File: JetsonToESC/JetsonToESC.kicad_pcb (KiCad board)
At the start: 2 copper layers, 70 x 50 mm, 37 parts, among them J1 Conn_01x12, J2 Conn_01x03, J3 Conn_01x02, J4 Screw_Terminal_01x01, J5 Screw_Terminal_01x01, U1 ESP32-C3_SUPERMINI_TH, U2 DS18B20, U3 LMR51420XDDCR, U4 MCP23018x-x-SS, U5 ACS759xCB-100B-PFF

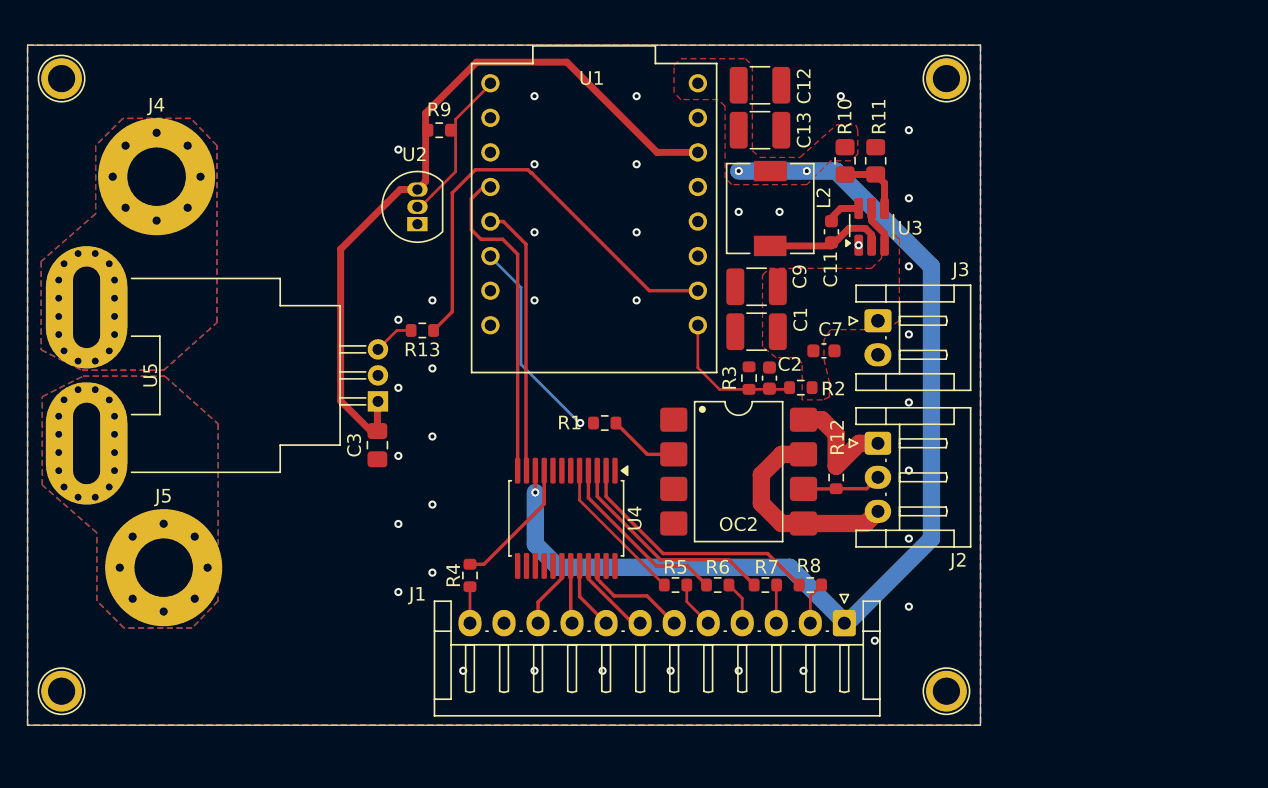
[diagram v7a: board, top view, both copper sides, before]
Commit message: Edit around current sensor
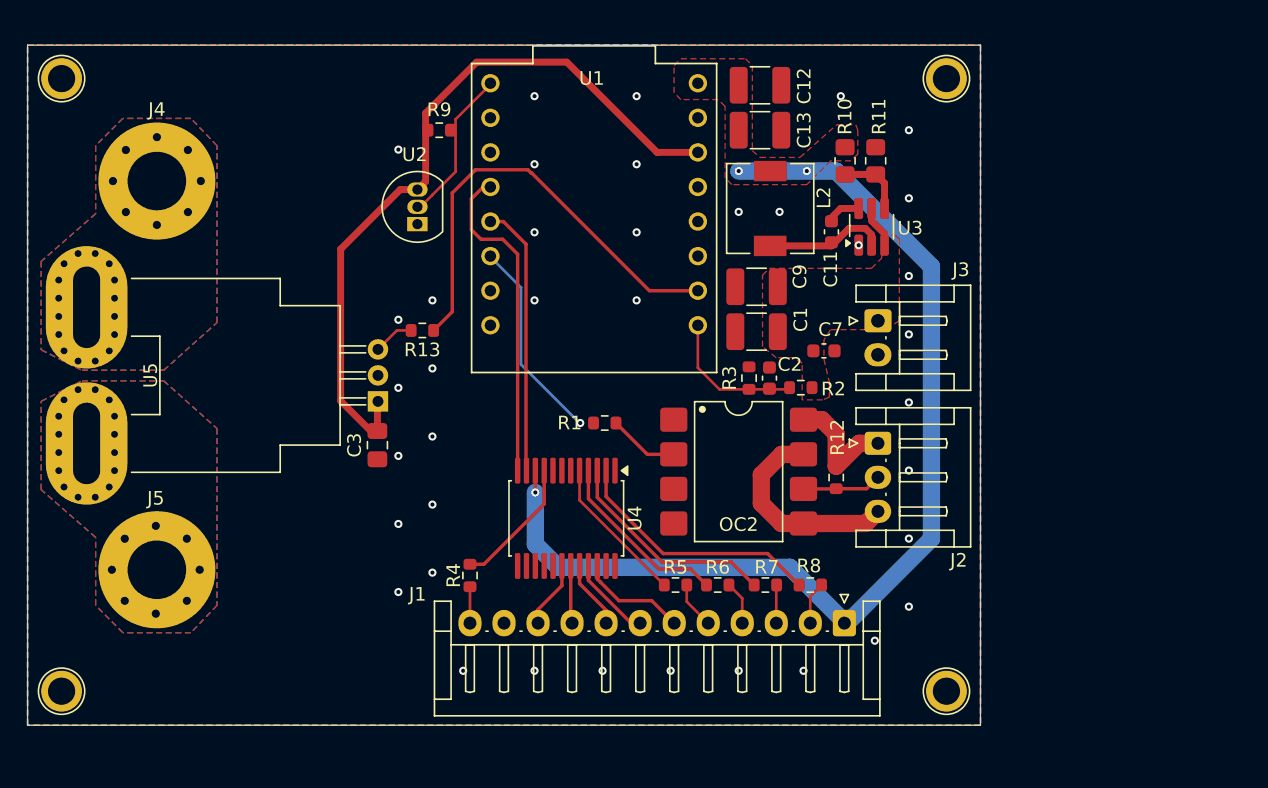
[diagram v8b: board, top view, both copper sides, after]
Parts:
- moved J5 0.60 mm to (119.4, 118.6)
- moved J4 0.32 mm to (119.5, 90.0)
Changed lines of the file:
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@@
 	(footprint "MountingHole:MountingHole_4.3mm_M4_Pad_Via"
 		(layer "F.Cu")
-		(at 119.480419 89.705419)
+		(at 119.5 90.025)
 		(descr "Mounting Hole 4.3mm, M4, generated by kicad-footprint-generator mountinghole.py")
 		(tags "mountinghole M4")
@@
 	(footprint "MountingHole:MountingHole_4.3mm_M4_Pad_Via"
 		(layer "F.Cu")
-		(at 120 118.425)
+		(at 119.419581 118.580419)
 		(descr "Mounting Hole 4.3mm, M4, generated by kicad-footprint-generator mountinghole.py")
 		(tags "mountinghole M4")
@@
 		)
 		(pad "1" thru_hole circle
-			(at 0 0)
-			(size 8.6 8.6)
-			(drill 4.3)
+			(at 0 3.225)
+			(size 0.9 0.9)
+			(drill 0.6)
 			(layers "*.Cu" "*.Mask")
 			(remove_unused_layers no)
@@
 		)
 		(pad "1" thru_hole circle
-			(at 0 3.225)
-			(size 0.9 0.9)
-			(drill 0.6)
+			(at 0.080419 0)
+			(size 8.6 8.6)
+			(drill 4.3)
 			(layers "*.Cu" "*.Mask")
 			(remove_unused_layers no)
@@
 	)
 	(segment
-		(start 147.5 120.958054)
-		(end 147.5 122.5)
+		(start 149.25 118.3)
+		(end 149.25 119.75)
 		(width 0.254)
 		(layer "F.Cu")
@@
 	)
 	(segment
-		(start 149.25 119.208054)
-		(end 147.5 120.958054)
+		(start 147.5 121.5)
+		(end 147.5 122.5)
 		(width 0.254)
 		(layer "F.Cu")
@@
 	)
 	(segment
-		(start 149.25 118.3)
-		(end 149.25 119.208054)
+		(start 149.25 119.75)
+		(end 147.5 121.5)
 		(width 0.254)
 		(layer "F.Cu")
@@
 	)
 	(segment
-		(start 150.55 120.55)
+		(start 150.55 118.3)
+		(end 150.55 119.6)
+		(width 0.254)
+		(layer "F.Cu")
+		(net 5)
+	)
+	(segment
+		(start 152.5 121.55)
 		(end 152.5 122.5)
 		(width 0.254)
@@
 	)
 	(segment
-		(start 150.55 118.3)
-		(end 150.55 120.55)
+		(start 150.55 119.6)
+		(end 152.5 121.55)
 		(width 0.254)
 		(layer "F.Cu")
@@
 	)
 	(via
-		(at 174.74 96.29)
+		(at 174.74 97)
 		(size 0.6)
 		(drill 0.3)
@@
 	)
 	(segment
-		(start 154.450001 122.5)
-		(end 155 122.5)
+		(start 151.2 118.3)
+		(end 151.2 119.36)
 		(width 0.254)
 		(layer "F.Cu")
@@
 	)
 	(segment
-		(start 151.2 119.249999)
-		(end 154.450001 122.5)
+		(start 154.34 122.5)
+		(end 155 122.5)
 		(width 0.254)
 		(layer "F.Cu")
@@
 	)
 	(segment
-		(start 151.2 118.3)
-		(end 151.2 119.249999)
+		(start 151.2 119.36)
+		(end 154.34 122.5)
 		(width 0.254)
 		(layer "F.Cu")
@@
 	)
 	(segment
-		(start 155.5 120.5)
-		(end 157.5 122.5)
+		(start 152.1 119.506531)
+		(end 153.443469 120.85)
 		(width 0.254)
 		(layer "F.Cu")
@@
 	)
 	(segment
-		(start 153.093469 120.5)
-		(end 155.5 120.5)
+		(start 152.1 119.499999)
+		(end 152.1 119.506531)
 		(width 0.254)
 		(layer "F.Cu")
@@
 	)
 	(segment
-		(start 152.1 119.506531)
-		(end 153.093469 120.5)
+		(start 151.85 118.3)
+		(end 151.85 119.249999)
 		(width 0.254)
 		(layer "F.Cu")
@@
 	)
 	(segment
-		(start 151.85 118.3)
-		(end 151.85 119.249999)
+		(start 155.85 120.85)
+		(end 157.5 122.5)
 		(width 0.254)
 		(layer "F.Cu")
@@
 	)
 	(segment
-		(start 152.1 119.499999)
-		(end 152.1 119.506531)
+		(start 153.443469 120.85)
+		(end 155.85 120.85)
 		(width 0.254)
 		(layer "F.Cu")
@@
 	)
 	(segment
-		(start 151.2 111.3)
-		(end 151.2 113.3)
+		(start 151.2 113.36)
+		(end 156.37 118.53)
 		(width 0.254)
 		(layer "F.Cu")
@@
 	)
 	(segment
-		(start 158.475 118.3)
+		(start 158.705 118.53)
 		(end 159.875 119.7)
 		(width 0.254)
@@
 	)
 	(segment
-		(start 151.2 113.3)
-		(end 156.2 118.3)
+		(start 156.37 118.53)
+		(end 158.705 118.53)
 		(width 0.254)
 		(layer "F.Cu")
@@
 	)
 	(segment
-		(start 156.2 118.3)
-		(end 158.475 118.3)
+		(start 151.2 111.3)
+		(end 151.2 113.36)
 		(width 0.254)
 		(layer "F.Cu")
@@
 	)
 	(segment
-		(start 156.5 117.845)
-		(end 151.85 113.195)
+		(start 156.5875 118)
+		(end 151.85 113.2625)
 		(width 0.254)
 		(layer "F.Cu")
@@
 	(segment
 		(start 163.375 119.7)
-		(end 161.52 117.845)
+		(end 161.675 118)
 		(width 0.254)
 		(layer "F.Cu")
@@
 	)
 	(segment
-		(start 161.52 117.845)
-		(end 156.5 117.845)
+		(start 161.675 118)
+		(end 156.5875 118)
 		(width 0.254)
 		(layer "F.Cu")
@@
 	)
 	(segment
-		(start 151.85 113.195)
+		(start 151.85 113.2625)
 		(end 151.85 111.3)
 		(width 0.254)
@@
 		(polygon
 			(pts
-				(xy 120.085 104.362962) (xy 124 107.862962) (xy 124 120.862962) (xy 122.085 122.862962) (xy 117.085 122.862962)
-				(xy 115.085 120.862962) (xy 115.085 115.862962) (xy 111.085 112.362962) (xy 111.085 105.862962)
-				(xy 114.085 104.362962)
+				(xy 120 104.7) (xy 123.915 108.2) (xy 123.915 121.2) (xy 122 123.2) (xy 117 123.2) (xy 115 121.2)
+				(xy 115 116.2) (xy 111 112.7) (xy 111 106.2) (xy 114 104.7)
 			)
 		)
